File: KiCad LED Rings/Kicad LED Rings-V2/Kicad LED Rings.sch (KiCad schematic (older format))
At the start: 27 parts, among them J1 Conn_01x02_Female, J2 Conn_01x02_Male, U1 LM3509SD_NOPB

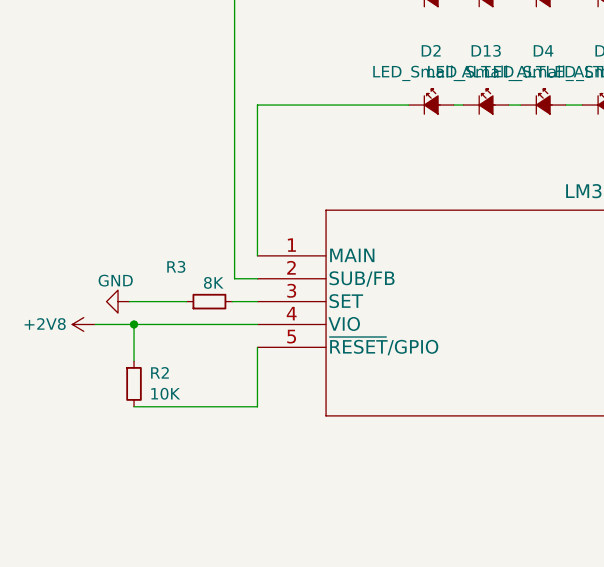
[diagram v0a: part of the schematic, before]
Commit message: Updated LED ring pcb
Changed Rset from 12k to 9.5k which can generate 25mA current for LEDs
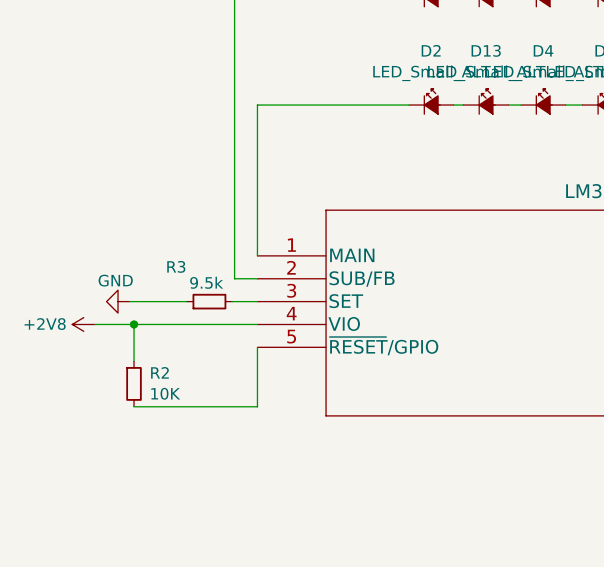
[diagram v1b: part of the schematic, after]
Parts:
- R3: value 8K -> 9.5k; PartNo. ERA-2AEB123X -> ERA-2AEB9531X
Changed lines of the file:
@@
 P 1820 2250
 F 0 "R3" V 1970 2350 50  0000 L CNN
-F 1 "8K" V 1900 2190 50  0000 L CNN
+F 1 "9.5k" V 1900 2190 50  0000 L CNN
 F 2 "Resistor_SMD:R_0402_1005Metric" H 1820 2250 50  0001 C CNN
 F 3 "https://www.digikey.com/product-detail/en/panasonic-electronic-components/ERA-2AEB123X/P12KDCCT-ND/1706209" H 1820 2250 50  0001 C CNN
-F 4 "ERA-2AEB123X" V 1770 2270 50  0001 C CNN "PartNo."
+F 4 "ERA-2AEB9531X" V 1770 2270 50  0001 C CNN "PartNo."
 	1    1820 2250
 	0    -1   -1   0
